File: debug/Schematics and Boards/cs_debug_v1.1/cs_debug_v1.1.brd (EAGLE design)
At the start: 81.3 x 62.2 mm, 217 parts, among them J1 J-JTAG-CORTEX_SMD, J19 Solar, J3 HIROSE-DF40_50-PIN_CONNECTORS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, J5 J-WURTH-USBC, Q10 2N7002P, Q3 FDN340P, Q4 2N7002P, Q5 FDN340P, Q6 2N7002P, Q7 FDN340P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

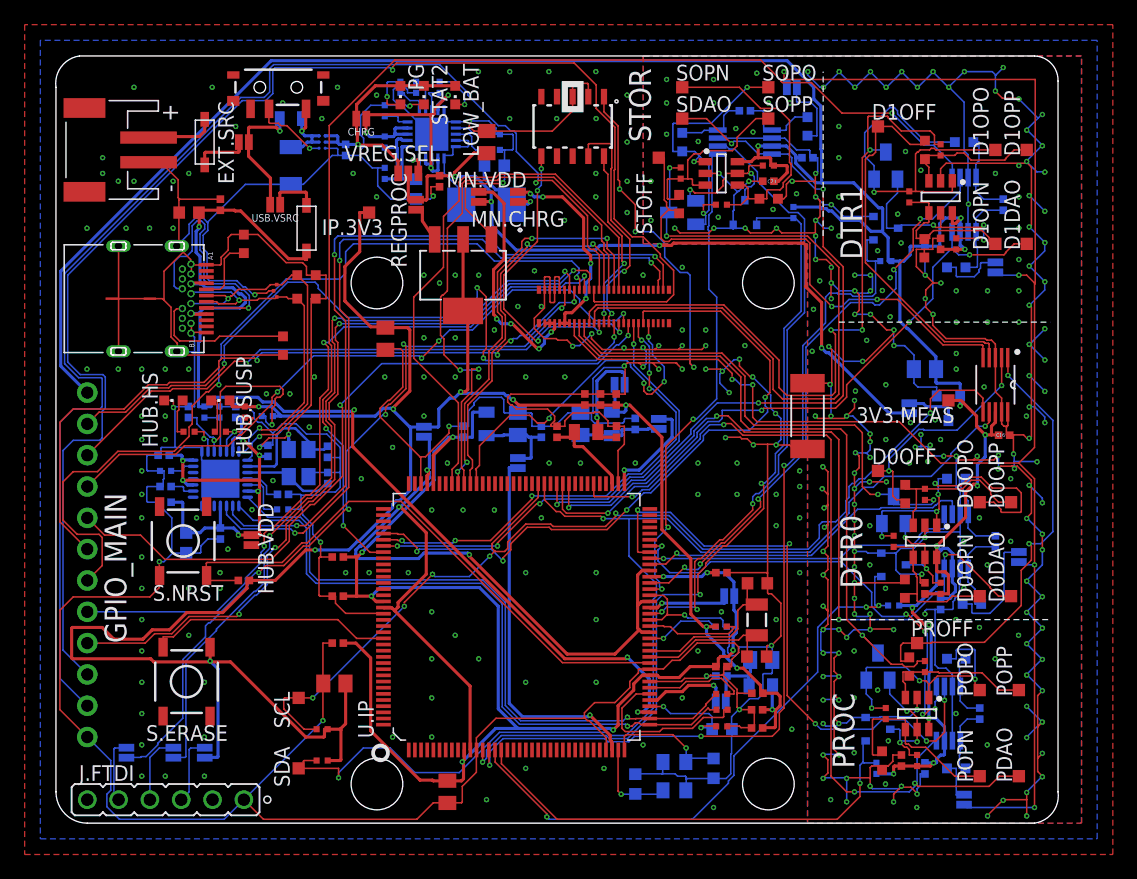
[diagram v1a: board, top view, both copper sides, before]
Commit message: Update files per design review and regenerate CAM
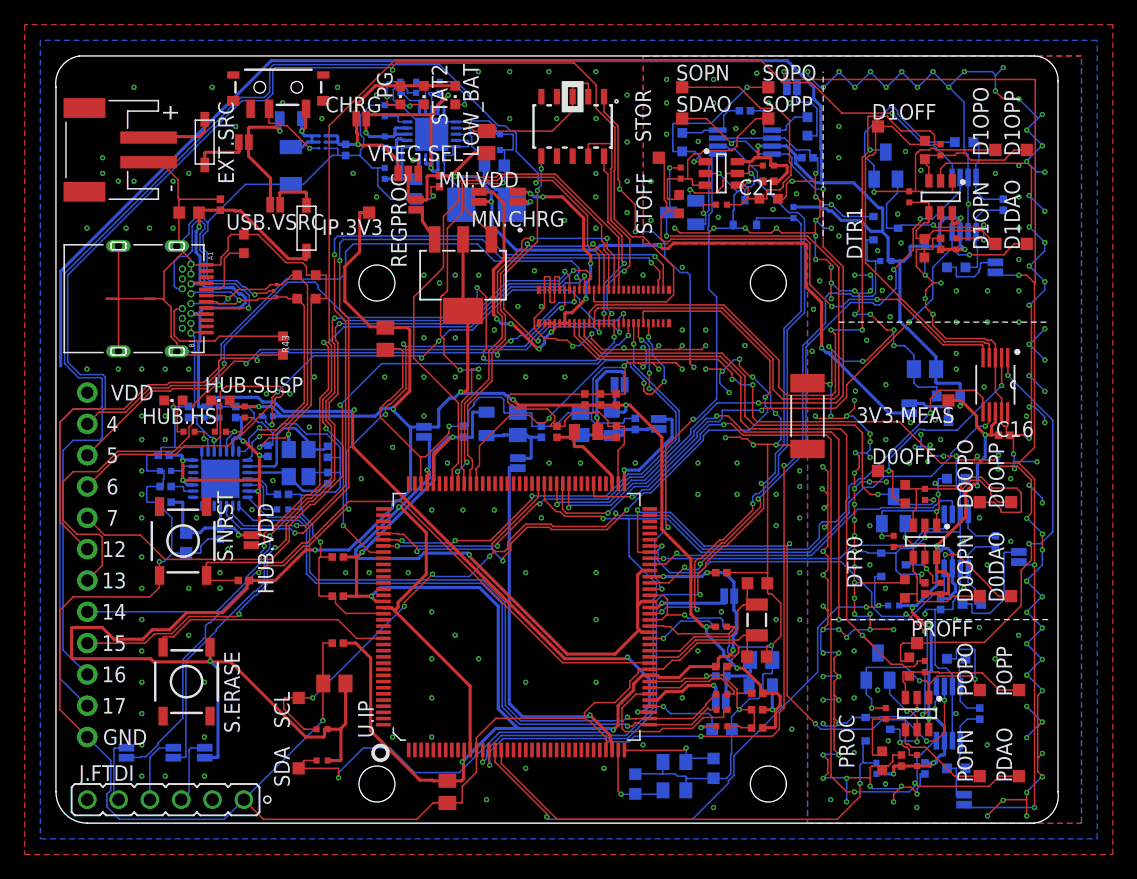
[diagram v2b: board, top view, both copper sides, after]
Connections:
- net 3V3_INSTR_MEAS: no longer JP1.1
- net V_SENSE_P: now also JP1.1
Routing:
- net 3V3_INSTR_MEAS: track 212.1 -> 209.0 mm
- net XIN: track 10.3 -> 8.80 mm
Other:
- board text added: "12"
- board text added: "13"
- board text added: "14"
- board text added: "15"
- board text added: "16"
- board text added: "17"
- board text added: "4"
- board text added: "5"
- board text added: "6"
- board text added: "7"
- board text added: "GND"
- board text added: "VDD"
- board text removed: "GPIO_MAIN"
- board text removed: "JTAG from base pokes into this region; keepout to minimize Z-height"

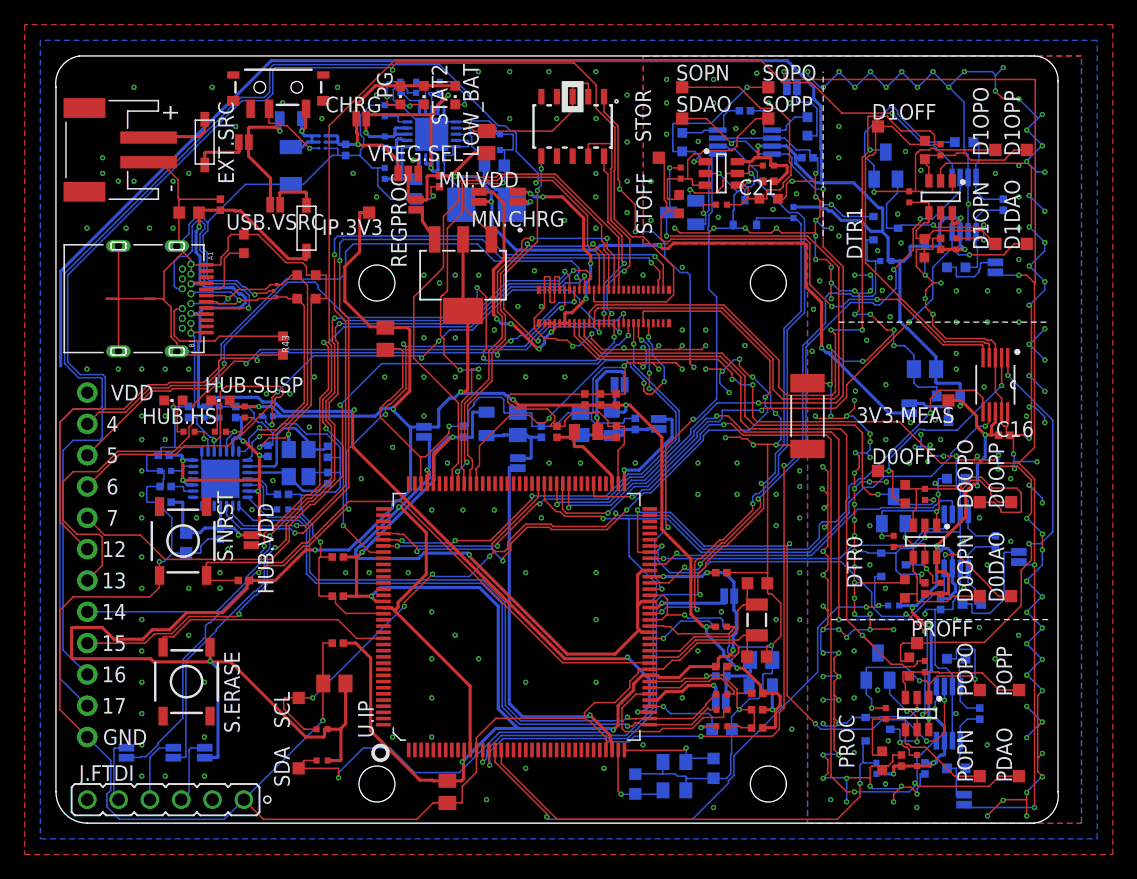
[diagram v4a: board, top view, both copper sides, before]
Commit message: DBG: Fix DFM issues for 7PCB
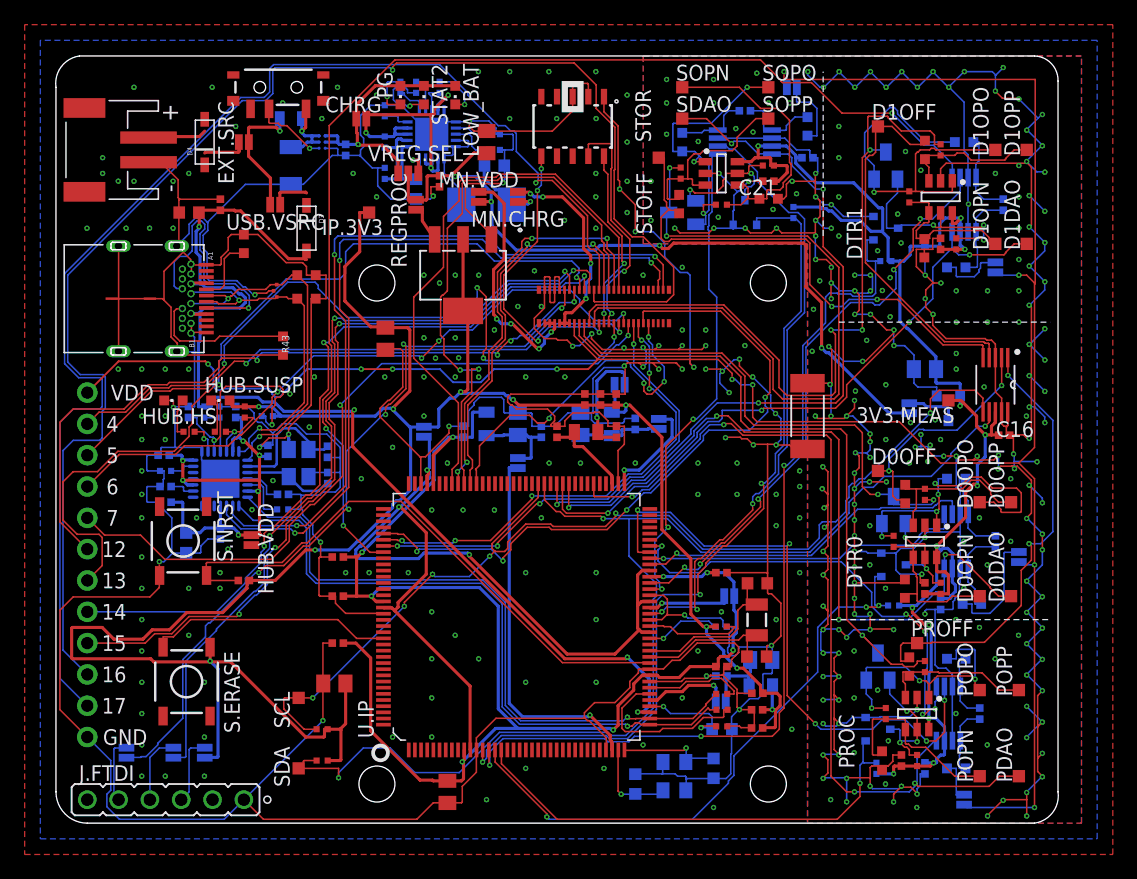
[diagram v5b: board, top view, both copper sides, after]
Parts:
- removed D1, D2: MBR120VLSFT3GOSCT-ND, adafruit:SOD-123
- added D3, D4: MBR120VLSFT3G, Diodes:SOD-123
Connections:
- net EXT_VIN: now also D4.A; no longer D1.A
- net N$15: now also D4.C; no longer D1.C
- net USBC_VBUS: now also D3.A; no longer D2.A
- net VUSB_DIODE: now also D3.C; no longer D2.C
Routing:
- net 3V3_INSTR_MEAS: track 209.0 -> 124.2 mm
- net V_SENSE_P: track 163.4 -> 210.3 mm, vias 9 -> 13
- net VUSB_DIODE: track 4.20 -> 3.19 mm
- net N$15: track 4.60 -> 3.63 mm
- net EXT_VIN: track 5.73 -> 4.77 mm
- net USBC_VBUS: track 90.8 -> 90.1 mm

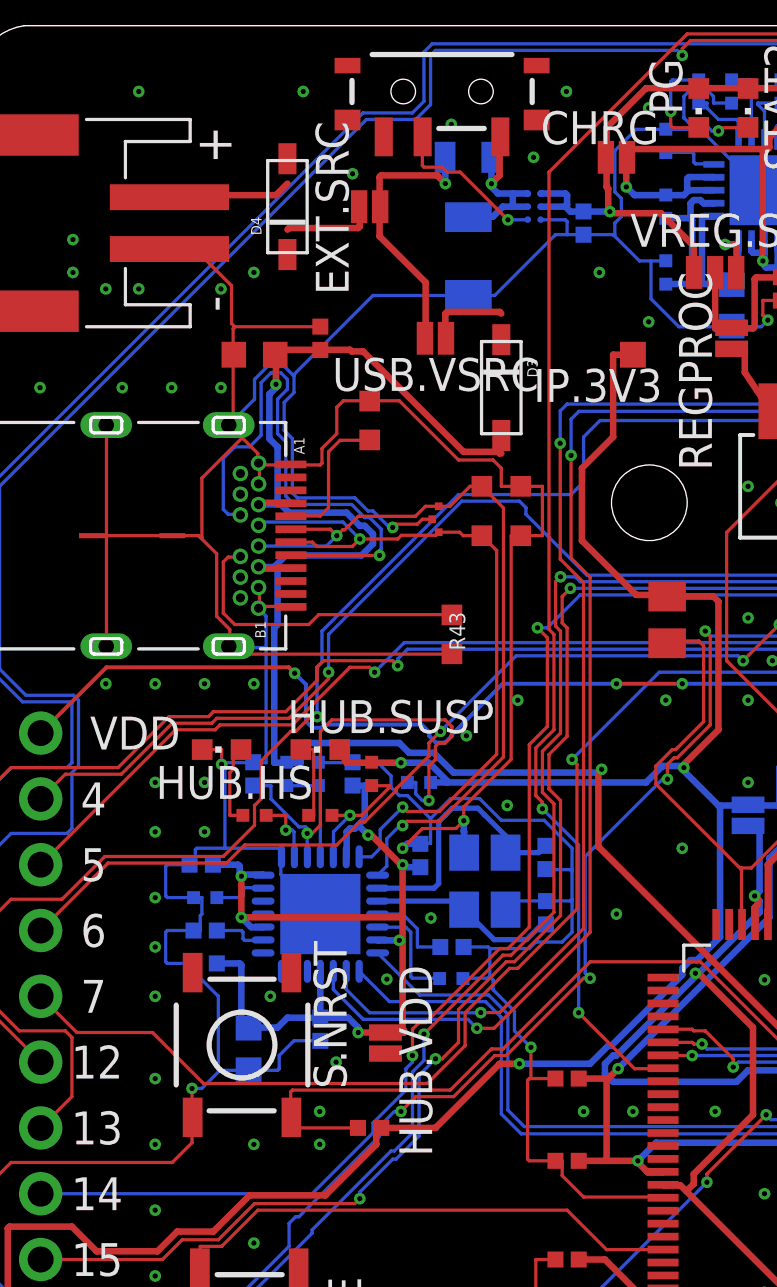
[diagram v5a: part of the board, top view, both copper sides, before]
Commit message: DTR: Regen gerbers for final design fixes in rev2.1
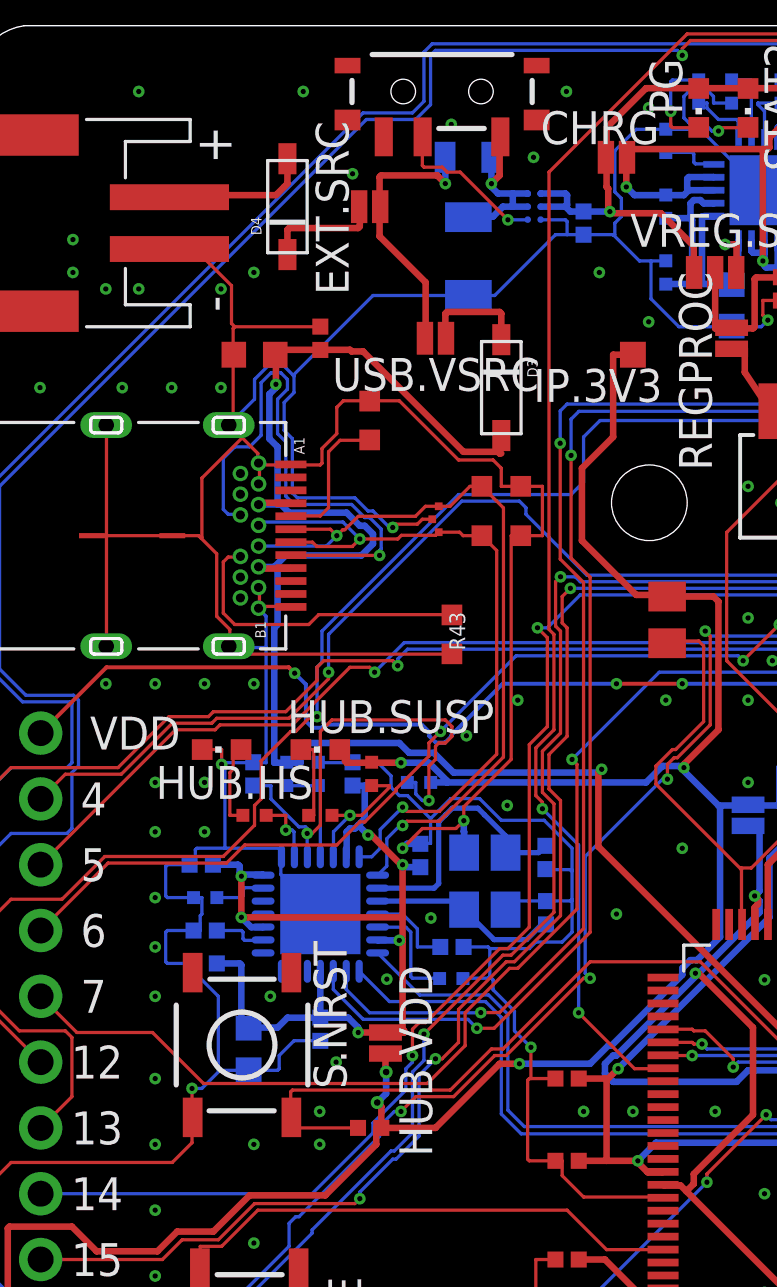
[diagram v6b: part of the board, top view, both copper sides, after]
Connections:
- removed net +3V3_INSTR_PROC: HUB.VDD.1
- net 3V3_INSTR_PROC: now also HUB.VDD.1
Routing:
- net 3V3_INSTR_PROC: track 197.6 -> 200.7 mm, vias 10 -> 12
- net VUSB_DIODE: track 3.19 -> 4.20 mm
- net EXT_VIN: track 4.77 -> 5.73 mm
- net N$15: track 3.63 -> 4.60 mm
- net USBC_VBUS: track 90.1 -> 90.8 mm
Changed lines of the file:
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@@
 <wire x1="-9.525" y1="49.7205" x2="-9.525" y2="49.715" width="0.254" layer="1"/>
 <wire x1="-11.2395" y1="49.53" x2="-11.265" y2="49.53" width="0.254" layer="1"/>
-<wire x1="-2.6035" y1="45.72" x2="-2.54" y2="45.72" width="0.254" layer="1"/>
+<wire x1="-2.54" y1="45.72" x2="-2.6035" y2="45.72" width="0.254" layer="1"/>
 <wire x1="-2.667" y1="45.7835" x2="-2.6035" y2="45.72" width="0.254" layer="1"/>
 <wire x1="-4.0005" y1="45.7835" x2="-2.667" y2="45.7835" width="0.254" layer="1"/>
@@
 <via x="-11.2395" y="48.387" extent="1-16" drill="0.2"/>
 <contactref element="D3" pad="A"/>
-<wire x1="-2.54" y1="45.72" x2="-2.54" y2="46.41" width="0" layer="19" extent="1-1"/>
+<wire x1="-2.6035" y1="45.72" x2="-2.6035" y2="46.3465" width="0.254" layer="1"/>
+<wire x1="-2.6035" y1="46.3465" x2="-2.54" y2="46.41" width="0.254" layer="1"/>
 </signal>
 <signal name="3V3_INSTR_PROC" class="1">
@@
 <wire x1="5.842" y1="40.005" x2="5.6532" y2="40.1938" width="0.254" layer="1"/>
 <wire x1="5.6532" y1="40.1938" x2="3.8608" y2="40.1938" width="0.254" layer="1"/>
+<contactref element="HUB.VDD" pad="1"/>
+<wire x1="-7.17" y1="19.685" x2="-7.17" y2="20.505" width="0.254" layer="1"/>
+<via x="-7.329646875" y="20.664646875" extent="1-16" drill="0.25"/>
+<wire x1="-7.329646875" y1="20.664646875" x2="-6.985" y2="21.00929375" width="0.254" layer="16"/>
+<via x="-6.985" y="21.842" extent="1-16" drill="0.25"/>
+<wire x1="-6.985" y1="21.842" x2="-7.0104" y2="21.8674" width="0.254" layer="1"/>
+<wire x1="-7.0104" y1="21.8674" x2="-7.0104" y2="22.5552" width="0.254" layer="1"/>
+<wire x1="-7.17" y1="20.505" x2="-7.329646875" y2="20.664646875" width="0.254" layer="1"/>
+<wire x1="-6.985" y1="21.00929375" x2="-6.985" y2="21.842" width="0.254" layer="16"/>
 </signal>
 <signal name="XIN32">
@@
 <signal name="EXT_VIN" class="1">
 <contactref element="J19" pad="1"/>
-<wire x1="-11.2395" y1="55.6895" x2="-10.795" y2="56.134" width="0.254" layer="1"/>
+<wire x1="-11.2395" y1="55.6895" x2="-10.922" y2="56.007" width="0.254" layer="1"/>
 <wire x1="-14.1605" y1="55.6895" x2="-11.2395" y2="55.6895" width="0.254" layer="1"/>
 <wire x1="-14.224" y1="55.626" x2="-14.1605" y2="55.6895" width="0.254" layer="1"/>
@@
 <wire x1="-15.3035" y1="55.626" x2="-15.35" y2="55.61" width="0.254" layer="1"/>
 <contactref element="D4" pad="A"/>
-<wire x1="-10.795" y1="56.134" x2="-10.795" y2="57.095" width="0" layer="19" extent="1-1"/>
+<wire x1="-10.922" y1="56.007" x2="-10.795" y2="56.134" width="0.254" layer="1"/>
+<wire x1="-10.795" y1="56.134" x2="-10.795" y2="57.095" width="0.254" layer="1"/>
 </signal>
 <signal name="CHG_VPCC" class="1">
@@
 <signal name="N$15" class="1">
 <contactref element="EXT.SRC" pad="1"/>
-<wire x1="-10.7315" y1="54.4195" x2="-10.795" y2="54.356" width="0.254" layer="1"/>
 <wire x1="-8.0645" y1="54.4195" x2="-10.7315" y2="54.4195" width="0.254" layer="1"/>
 <wire x1="-8.001" y1="54.483" x2="-8.0645" y2="54.4195" width="0.254" layer="1"/>
@@
 <wire x1="-8.001" y1="55.245" x2="-8.0264" y2="55.245" width="0.254" layer="1"/>
 <contactref element="D4" pad="C"/>
-<wire x1="-10.795" y1="53.395" x2="-10.795" y2="54.356" width="0" layer="19" extent="1-1"/>
+<wire x1="-10.7315" y1="54.4195" x2="-10.795" y2="54.356" width="0.254" layer="1"/>
+<wire x1="-10.795" y1="54.356" x2="-10.795" y2="53.395" width="0.254" layer="1"/>
 </signal>
 <signal name="CC3">
@@
 <via x="-4.699" y="56.134" extent="1-16" drill="0.2"/>
 </signal>
-<signal name="+3V3_INSTR_PROC" class="1">
-<contactref element="HUB.VDD" pad="1"/>
-</signal>
 <signal name="USB_HUB_VDD" class="1">
 <contactref element="C54" pad="1"/>
@@
 <signal name="VUSB_DIODE" class="1">
 <contactref element="USB.VSRC" pad="1"/>
-<wire x1="-2.6035" y1="51.181" x2="-2.54" y2="51.1175" width="0.254" layer="1"/>
+<wire x1="-2.54" y1="51.1175" x2="-2.6035" y2="51.181" width="0.254" layer="1"/>
 <wire x1="-4.6355" y1="51.181" x2="-2.6035" y2="51.181" width="0.254" layer="1"/>
 <wire x1="-4.699" y1="51.1175" x2="-4.6355" y2="51.181" width="0.254" layer="1"/>
@@
 <wire x1="-4.699" y1="50.165" x2="-4.6736" y2="50.165" width="0.254" layer="1"/>
 <contactref element="D3" pad="C"/>
-<wire x1="-2.54" y1="50.11" x2="-2.54" y2="51.1175" width="0" layer="19" extent="1-1"/>
+<wire x1="-2.54" y1="50.11" x2="-2.54" y2="51.1175" width="0.254" layer="1"/>
 </signal>
 <signal name="N$3">
